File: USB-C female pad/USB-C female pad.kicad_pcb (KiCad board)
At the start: 2 copper layers, 21.2 x 21.2 mm, 5 parts, among them J1 USB_C_Receptacle_PowerOnly_6P, J2 Conn_01x02_Socket

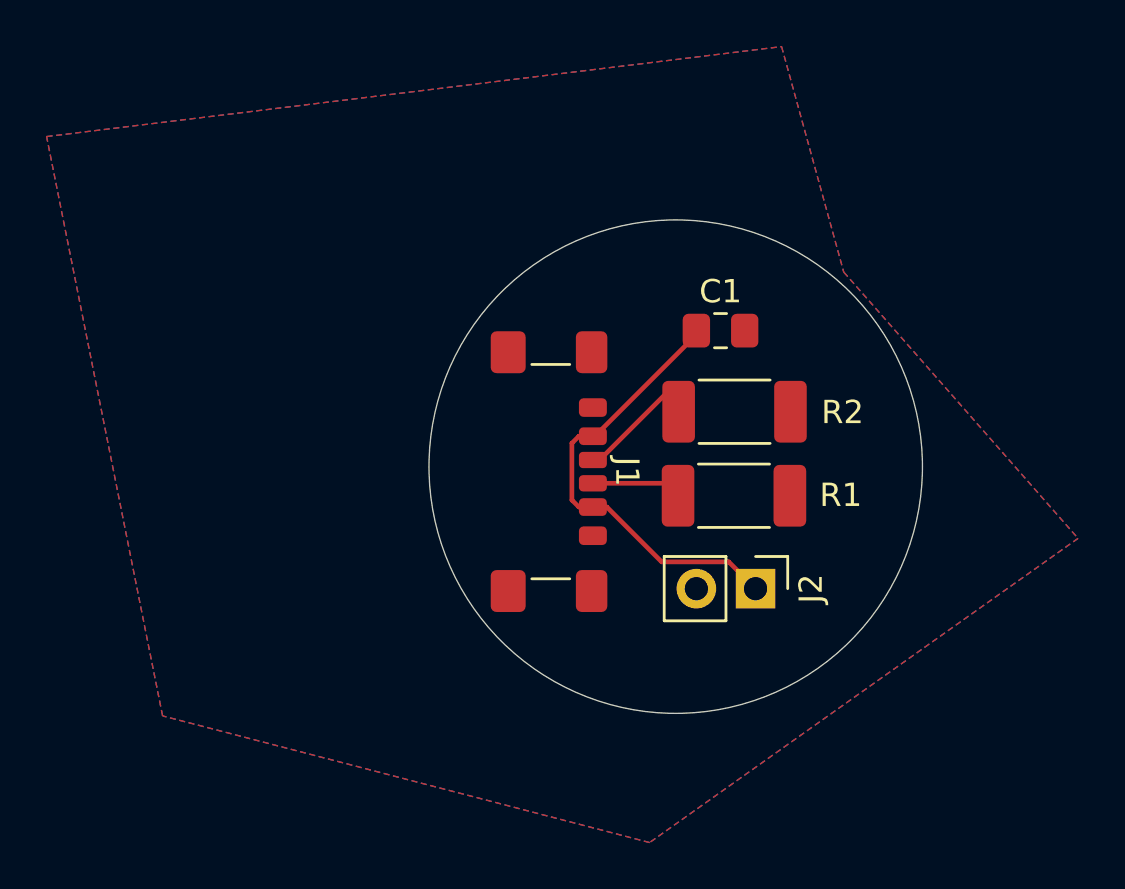
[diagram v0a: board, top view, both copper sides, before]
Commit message: Small trace changes
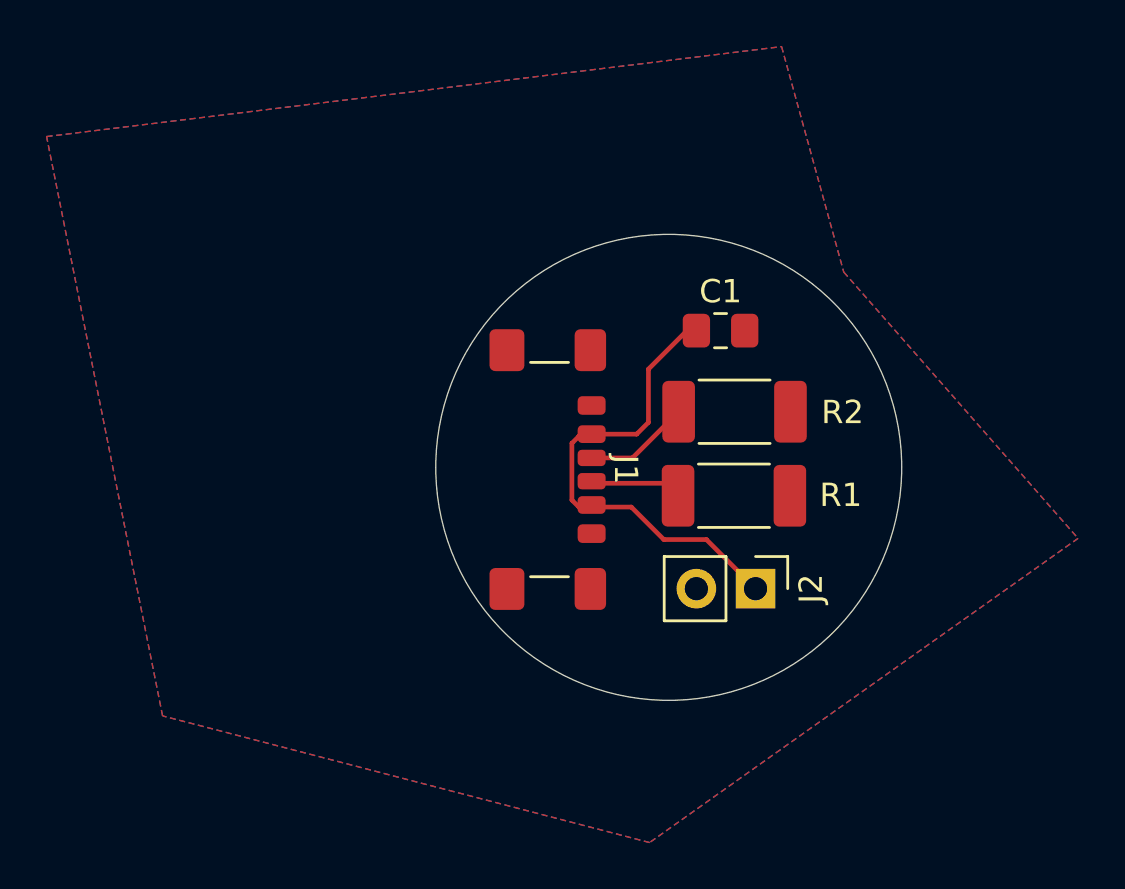
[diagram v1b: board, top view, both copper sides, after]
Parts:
- moved J1 0.10 mm to (130.4, 89.6)
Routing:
- net Net-(J2-Pin_1): track 19.3 -> 20.9 mm
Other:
- board size 21.2 x 21.2 mm -> 20 x 20 mm
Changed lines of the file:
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@@
 			(outputformat 1)
 			(mirror no)
-			(drillshape 1)
+			(drillshape 0)
 			(scaleselection 1)
 			(outputdirectory "")
@@
 	(footprint "Connector_USB:USB_C_Receptacle_GCT_USB4135-GF-A_6P_TopMnt_Horizontal"
 		(layer "F.Cu")
-		(at 130.4727 89.6932 -90)
+		(at 130.4191 89.6044 -90)
 		(descr "USB Type C Receptacle, GCT, power-only, 6P, top mounted, horizontal, 3A: https://gct.co/files/drawings/usb4135.pdf")
 		(tags "USB C Type-C Receptacle SMD USB Power-only Charging-only 6P 6C USB4135-GF-A")
@@
 	)
 	(gr_circle
-		(center 137.0606 89.4788)
-		(end 126.4727 89.6932)
+		(center 136.7612 89.5096)
+		(end 146.7612 89.5096)
 		(stroke
 			(width 0.05)
-			(type default)
+			(type solid)
 		)
 		(fill no)
@@
 	)
 	(segment
-		(start 137.9474 83.815064)
-		(end 133.589264 88.1732)
-		(width 0.2)
-		(layer "F.Cu")
-		(net 2)
-	)
-	(segment
-		(start 133.5052 91.2132)
+		(start 133.4516 88.0844)
+		(end 135.3848 88.0844)
+		(width 0.2)
+		(layer "F.Cu")
+		(net 2)
+	)
+	(segment
+		(start 135.1552 91.2132)
+		(end 136.5504 92.6084)
+		(width 0.2)
+		(layer "F.Cu")
+		(net 2)
+	)
+	(segment
+		(start 132.6042 88.4742)
+		(end 132.6042 90.9122)
+		(width 0.2)
+		(layer "F.Cu")
+		(net 2)
+	)
+	(segment
+		(start 135.89 87.5792)
+		(end 135.89 85.2932)
+		(width 0.2)
+		(layer "F.Cu")
+		(net 2)
+	)
+	(segment
+		(start 136.5504 92.6084)
+		(end 138.3792 92.6084)
+		(width 0.2)
+		(layer "F.Cu")
+		(net 2)
+	)
+	(segment
+		(start 132.6042 90.9122)
 		(end 132.9052 91.2132)
 		(width 0.2)
@@
 	(segment
 		(start 133.589264 88.1732)
-		(end 133.5052 88.1732)
+		(end 132.9052 88.1732)
 		(width 0.2)
 		(layer "F.Cu")
@@
 	(segment
 		(start 132.9052 91.2132)
-		(end 132.6042 90.9122)
-		(width 0.2)
-		(layer "F.Cu")
-		(net 2)
-	)
-	(segment
-		(start 136.4576 93.5656)
-		(end 139.3364 93.5656)
-		(width 0.2)
-		(layer "F.Cu")
-		(net 2)
-	)
-	(segment
-		(start 139.3364 93.5656)
-		(end 140.4874 94.7166)
-		(width 0.2)
-		(layer "F.Cu")
-		(net 2)
-	)
-	(segment
-		(start 133.5052 91.2132)
-		(end 134.1052 91.2132)
-		(width 0.2)
-		(layer "F.Cu")
-		(net 2)
-	)
-	(segment
-		(start 132.6042 88.4742)
-		(end 132.9052 88.1732)
-		(width 0.2)
-		(layer "F.Cu")
-		(net 2)
-	)
-	(segment
-		(start 132.6042 90.9122)
+		(end 135.1552 91.2132)
+		(width 0.2)
+		(layer "F.Cu")
+		(net 2)
+	)
+	(segment
+		(start 132.9052 88.1732)
 		(end 132.6042 88.4742)
+		(width 0.2)
+		(layer "F.Cu")
+		(net 2)
+	)
+	(segment
+		(start 137.541 83.6422)
+		(end 137.9474 83.6422)
 		(width 0.2)
 		(layer "F.Cu")
@@
 	)
 	(segment
-		(start 132.9052 88.1732)
-		(end 133.5052 88.1732)
-		(width 0.2)
-		(layer "F.Cu")
-		(net 2)
-	)
-	(segment
-		(start 134.1052 91.2132)
-		(end 136.4576 93.5656)
-		(width 0.2)
-		(layer "F.Cu")
-		(net 2)
-	)
-	(segment
-		(start 136.9574 86.0298)
-		(end 133.794 89.1932)
+		(start 135.3848 88.0844)
+		(end 135.89 87.5792)
+		(width 0.2)
+		(layer "F.Cu")
+		(net 2)
+	)
+	(segment
+		(start 135.89 85.2932)
+		(end 137.541 83.6422)
+		(width 0.2)
+		(layer "F.Cu")
+		(net 2)
+	)
+	(segment
+		(start 138.3792 92.6084)
+		(end 140.4874 94.7166)
+		(width 0.2)
+		(layer "F.Cu")
+		(net 2)
+	)
+	(segment
+		(start 133.4516 89.1044)
+		(end 135.2036 89.1044)
 		(width 0.2)
 		(layer "F.Cu")
@@
 		(width 0.2)
 		(layer "F.Cu")
+		(net 3)
+	)
+	(segment
+		(start 135.2036 89.1044)
+		(end 137.186 87.122)
+		(width 0.2)
+		(layer "F.Cu")

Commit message: Add SP0503BAHTG to USB-C pad
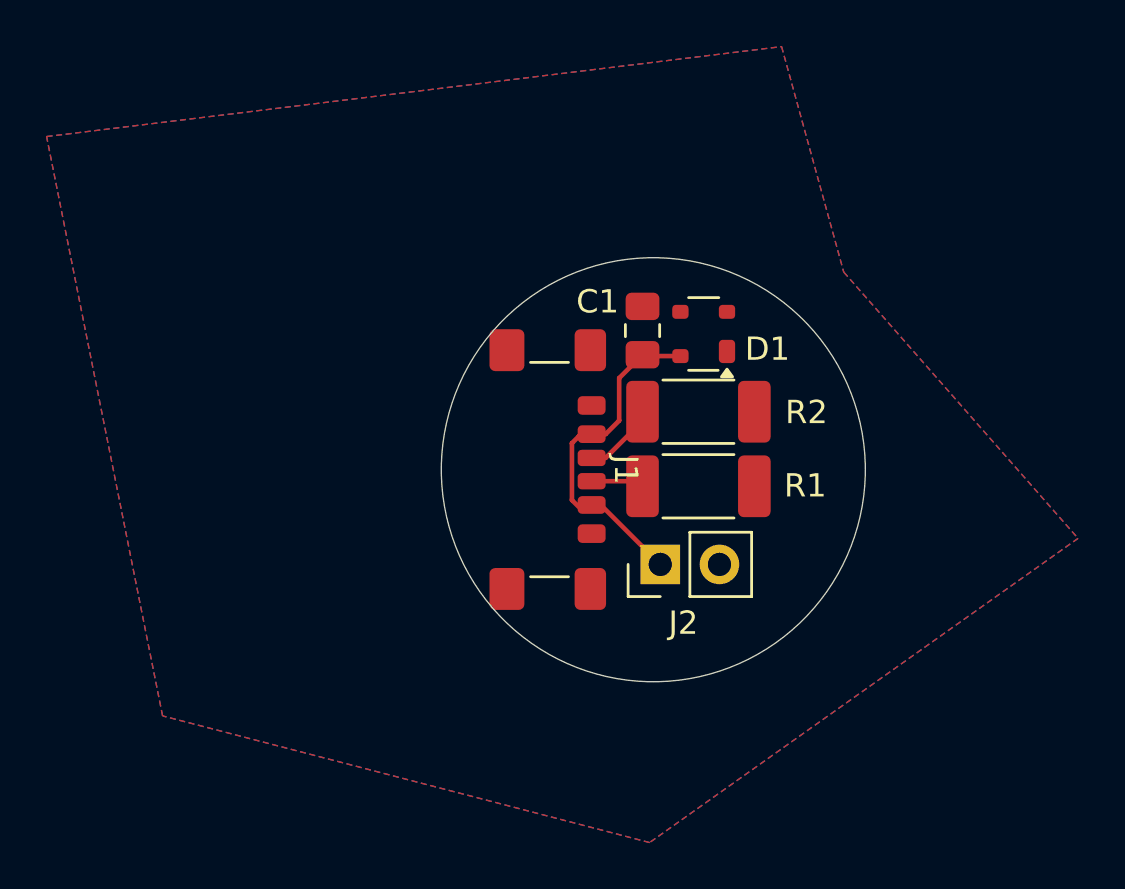
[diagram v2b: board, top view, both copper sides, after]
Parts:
- added D1: SP0503BAHT, Package_TO_SOT_SMD:SOT-143, F.Cu at (138.3, 83.8)
- moved J2 4.22 mm to (136.4, 93.7), turned to 90 degrees
- moved C1 3.35 mm to (135.6, 83.6), turned to 90 degrees
- moved R1 1.58 mm to (138.0, 90.3)
- moved R2 1.55 mm to (138.0, 87.1)
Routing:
- net Net-(J2-Pin_1): track 20.9 -> 14.3 mm
- net Net-(J1-CC2): track 3.88 -> 2.27 mm
- net Net-(J1-CC1): track 4.84 -> 3.53 mm
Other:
- board size 20 x 20 mm -> 18.2 x 18.2 mm
